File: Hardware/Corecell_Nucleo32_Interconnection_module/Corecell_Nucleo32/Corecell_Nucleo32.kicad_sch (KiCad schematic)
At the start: 3 parts, among them IC1 PCI_EXPRESS_CARD, J1 Conn_02x20_Odd_Even, U1 ESP32-DEVKITC-32D

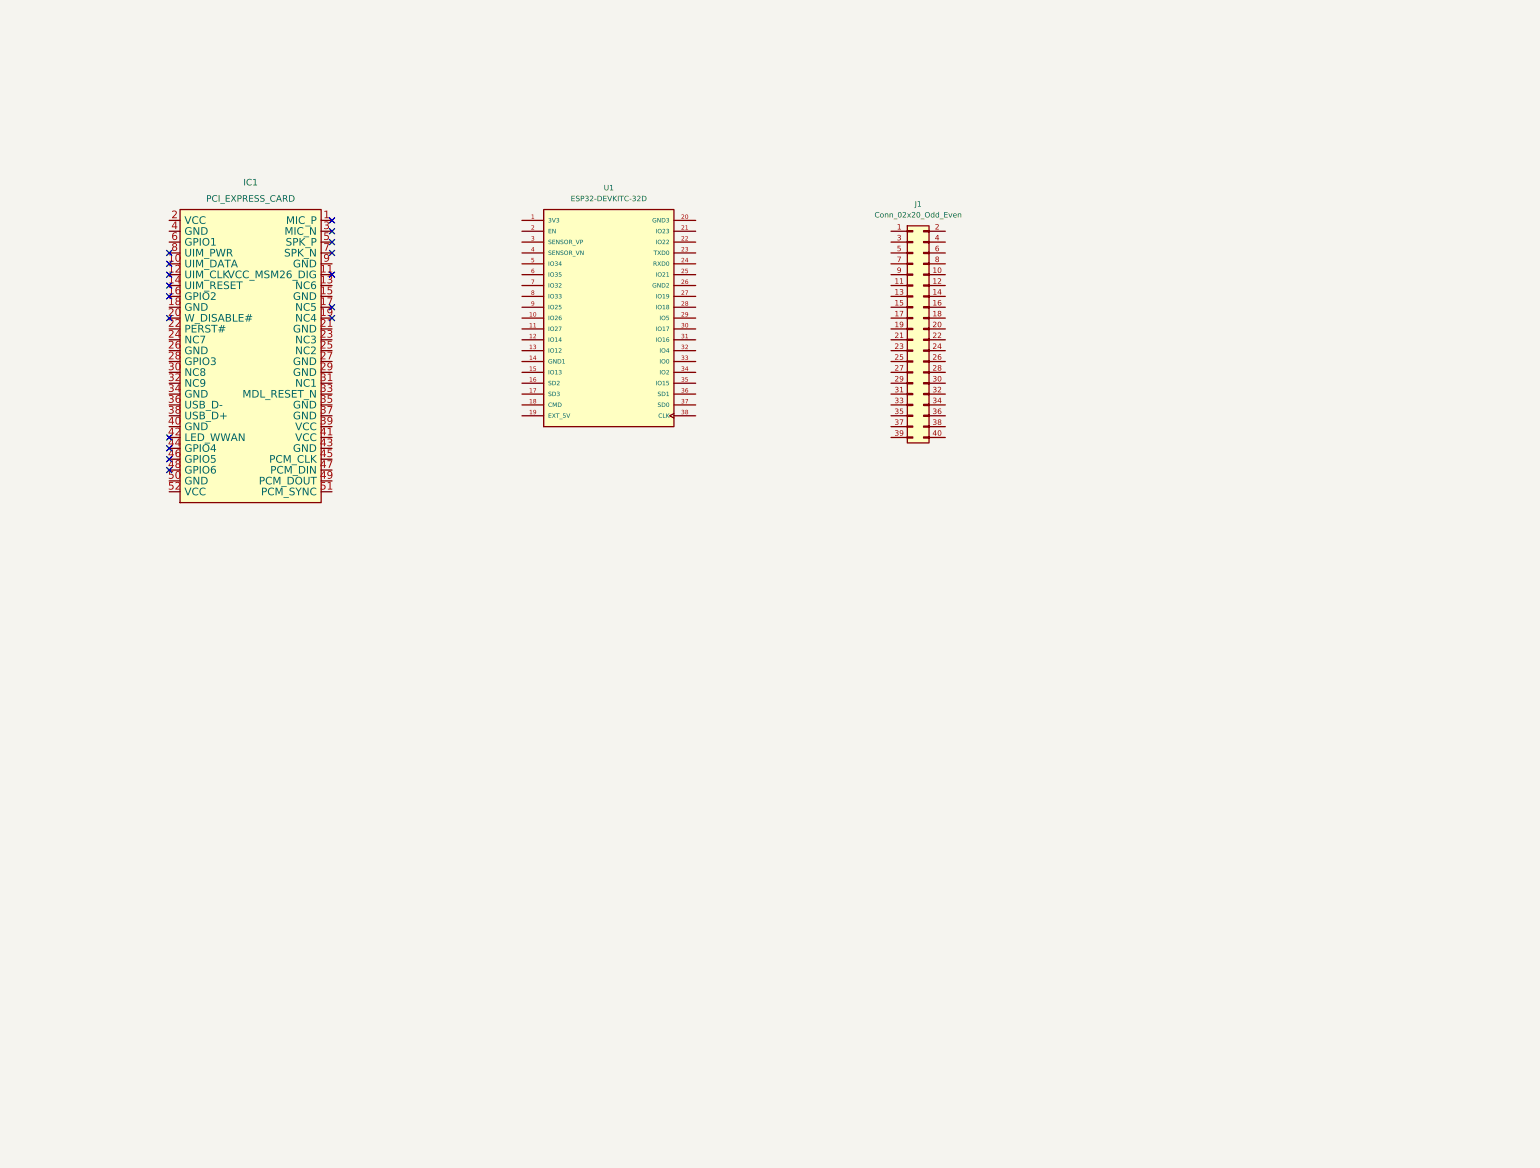
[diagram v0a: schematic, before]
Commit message: Some libs were made and added to schematic, the schematic is almost ready, fixing some warnings
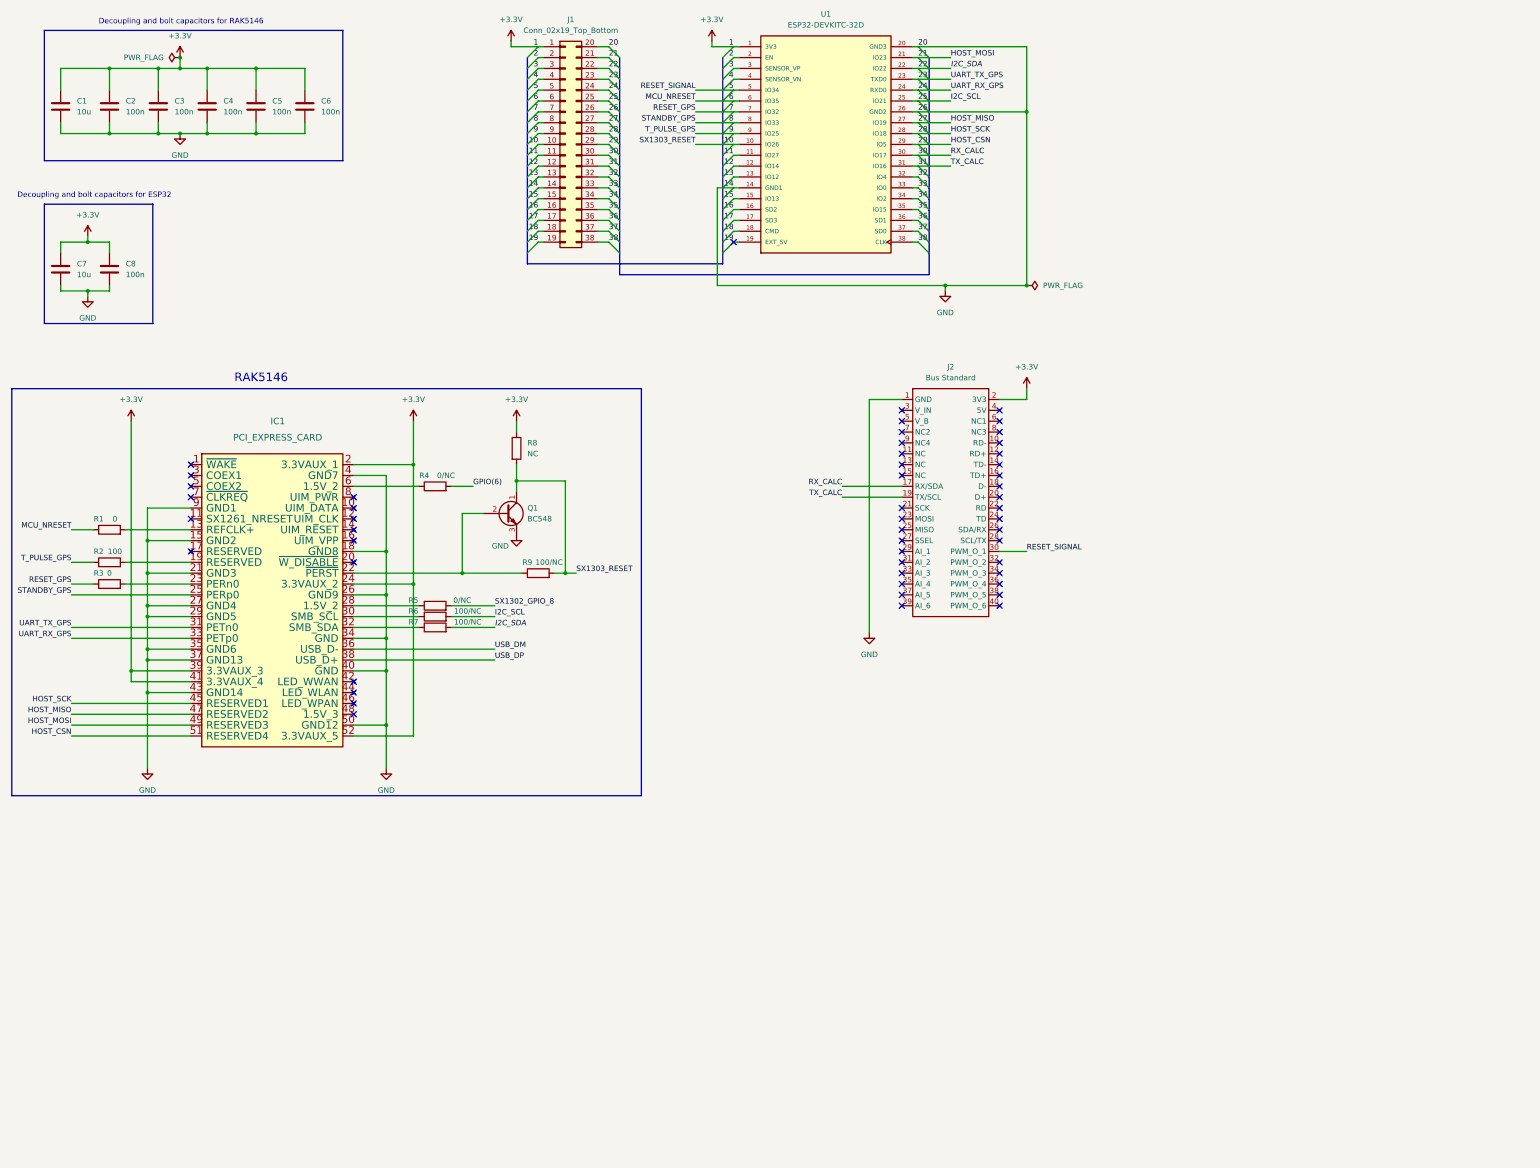
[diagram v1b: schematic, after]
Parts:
- removed J1: Conn_02x20_Odd_Even, symbol Connector_Generic:Conn_02x20_Odd_Even
- added C1, C7: 10u, symbol Device:C
- added C2, C3, C4, C5, C6, C8: 100n, symbol Device:C
- added J1: Conn_02x19_Top_Bottom, symbol Connector_Generic:Conn_02x19_Top_Bottom
- added J2: Bus Standard, symbol Corecell_Intercon_Board:Flatsat_conn
- added Q1: BC548, Package_TO_SOT_THT:TO-92_Inline, symbol Transistor_BJT:BC548
- added R1, R3: 0, symbol Device:R
- added R2: 100, symbol Device:R
- added R4, R5: 0/NC, symbol Device:R
- added R6, R7, R9: 100/NC, symbol Device:R
- added R8: NC, symbol Device:R
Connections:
- net +3V3: now reaches U1.1 (3V3)
- net +3V3: now also IC1.2 (3.3VAUX_1), IC1.24 (3.3VAUX_2), IC1.39 (3.3VAUX_3), IC1.41 (3.3VAUX_4), IC1.52 (3.3VAUX_5), C1.1, C2.1, C3.1, C4.1, C5.1, C6.1, C7.1, C8.1, J1.1 (Pin_1), J2.2 (3V3), R8.1
- net 10: now reaches U1.10 (IO26)
- net 10: now also J1.10 (Pin_10), Q1.1 (C), R8.2, R9.2
- net 11: now reaches U1.11 (IO27)
- net 11: now also J1.11 (Pin_11)
- net 12: now reaches U1.12 (IO14)
- net 12: now also J1.12 (Pin_12)
- net 13: now reaches U1.13 (IO12)
- net 13: now also J1.13 (Pin_13)
- net GND: now reaches U1.14 (GND1)
- net GND: now also IC1.15 (GND2), IC1.18 (GND8), IC1.21 (GND3), IC1.26 (GND9), IC1.27 (GND4), IC1.29 (GND5), IC1.34 (GND), IC1.35 (GND6), IC1.37 (GND13), IC1.4 (GND7), IC1.40 (GND), IC1.43 (GND14), IC1.50 (GND12), IC1.9 (GND1), U1.20 (GND3), U1.26 (GND2), C1.2, C2.2, C3.2, C4.2, C5.2, C6.2, C7.2, C8.2, J1.14 (Pin_14), J1.20 (Pin_20), J1.26 (Pin_26), J2.1 (GND), Q1.3 (E)
- net 15: now reaches U1.15 (IO13)
- net 15: now also J1.15 (Pin_15)
- net 16: now reaches U1.16 (SD2)
- net 16: now also J1.16 (Pin_16)
- net 17: now reaches U1.17 (SD3)
- net 17: now also J1.17 (Pin_17)
- net 18: now reaches U1.18 (CMD)
- net 18: now also J1.18 (Pin_18)
- net 19: now reaches U1.19 (EXT_5V)
- net 19: now also J1.19 (Pin_19)
- net 2: now reaches U1.2 (EN)
- net 2: now also J1.2 (Pin_2)
- net 21: now reaches U1.21 (IO23)
- net 21: now also IC1.49 (RESERVED3), J1.21 (Pin_21)
- net 22: now reaches U1.22 (IO22)
- net 22: now also J1.22 (Pin_22), R7.2
- net 23: now reaches U1.23 (TXD0)
- net 23: now also IC1.31 (PETn0), J1.23 (Pin_23)
- net 24: now reaches U1.24 (RXD0)
- net 24: now also IC1.33 (PETp0), J1.24 (Pin_24)
- net 25: now reaches U1.25 (IO21)
- net 25: now also J1.25 (Pin_25), R6.2
- net 27: now reaches U1.27 (IO19)
- net 27: now also IC1.47 (RESERVED2), J1.27 (Pin_27)
- net 28: now reaches U1.28 (IO18)
- net 28: now also IC1.45 (RESERVED1), J1.28 (Pin_28)
- net 29: now reaches U1.29 (IO5)
- net 29: now also IC1.51 (RESERVED4), J1.29 (Pin_29)
- net 3: now reaches U1.3 (SENSOR_VP)
- net 3: now also J1.3 (Pin_3)
- net 30: now reaches U1.30 (IO17)
- net 30: now also J1.30 (Pin_30), J2.17 (RX/SDA)
- net 31: now reaches U1.31 (IO16)
- net 31: now also J1.31 (Pin_31), J2.19 (TX/SCL)
- net 32: now reaches U1.32 (IO4)
- net 32: now also J1.32 (Pin_32)
- net 33: now reaches U1.33 (IO0)
- net 33: now also J1.33 (Pin_33)
- net 34: now reaches U1.34 (IO2)
- net 34: now also J1.34 (Pin_34)
- net 35: now reaches U1.35 (IO15)
- net 35: now also J1.35 (Pin_35)
- net 36: now reaches U1.36 (SD1)
- net 36: now also J1.36 (Pin_36)
- net 37: now reaches U1.37 (SD0)
- net 37: now also J1.37 (Pin_37)
- net 38: now reaches U1.38 (CLK)
- net 38: now also J1.38 (Pin_38)
- net 4: now reaches U1.4 (SENSOR_VN)
- net 4: now also J1.4 (Pin_4)
- net 5: now reaches U1.5 (IO34)
- net 5: now also J1.5 (Pin_5), J2.30 (PWM_O_1)
- net 6: now reaches U1.6 (IO35)
- net 6: now also J1.6 (Pin_6), R1.1
- net 7: now reaches U1.7 (IO32)
- net 7: now also J1.7 (Pin_7), R3.1
- net 8: now reaches U1.8 (IO33)
- net 8: now also IC1.25 (PERp0), J1.8 (Pin_8)
- net 9: now reaches U1.9 (IO25)
- net 9: now also J1.9 (Pin_9), R2.1
- net at IC1.13 (REFCLK+): now also R1.2
- net at IC1.19 (RESERVED): now also R2.2
- net at IC1.22 (~{PERST}): now also Q1.2 (B), R9.1
- net at IC1.23 (PERn0): now also R3.2
- net at IC1.28 (1.5V_2): now also R5.1
- net at IC1.30 (SMB_SCL): now also R6.1
- net at IC1.32 (SMB_SDA): now also R7.1
- net USB_DM: now reaches IC1.36 (USB_D-)
- net USB_DP: now reaches IC1.38 (USB_D+)
- net at IC1.6 (1.5V_2): now also R4.1
- new net GPIO(6): R4.2
- new net SX1302_GPIO_8: R5.2
- no-connect marks 17 -> 52
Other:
- note added: "Decoupling and bolt capacitors for ESP32"
- note added: "Decoupling and bolt capacitors for RAK5146"
- note added: "RAK5146"
- moved on the sheet: U1

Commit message: The base of schematic is completly connected, there is no error, no warning neither by ERC. After some debug connector will be added to give access to some critic connections points, like UART and others.
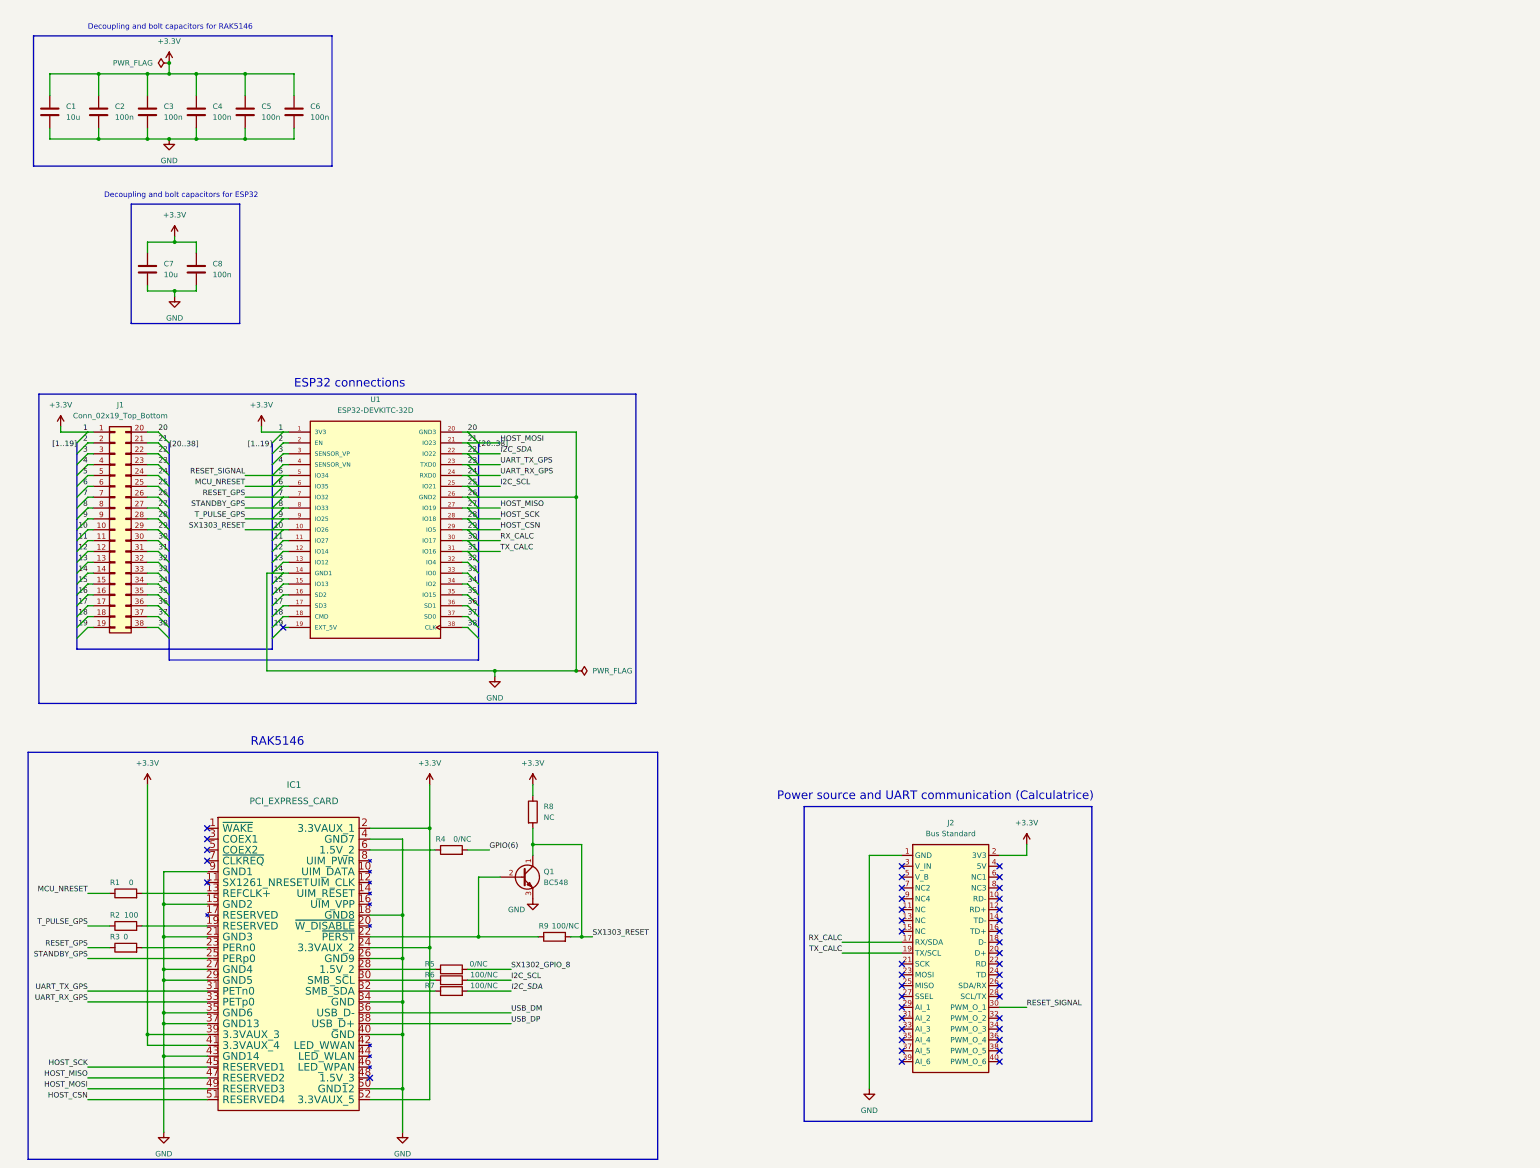
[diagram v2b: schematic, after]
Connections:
- no-connect marks 52 -> 42
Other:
- note added: "ESP32 connections"
- note added: "Power source and UART communication (Calculatrice)"
- moved on the sheet: C1, C2, C3, C4, C5, C6, C7, C8, IC1, J1, Q1, R1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

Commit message: Communication debug grooves were added. Some reset jumpers also
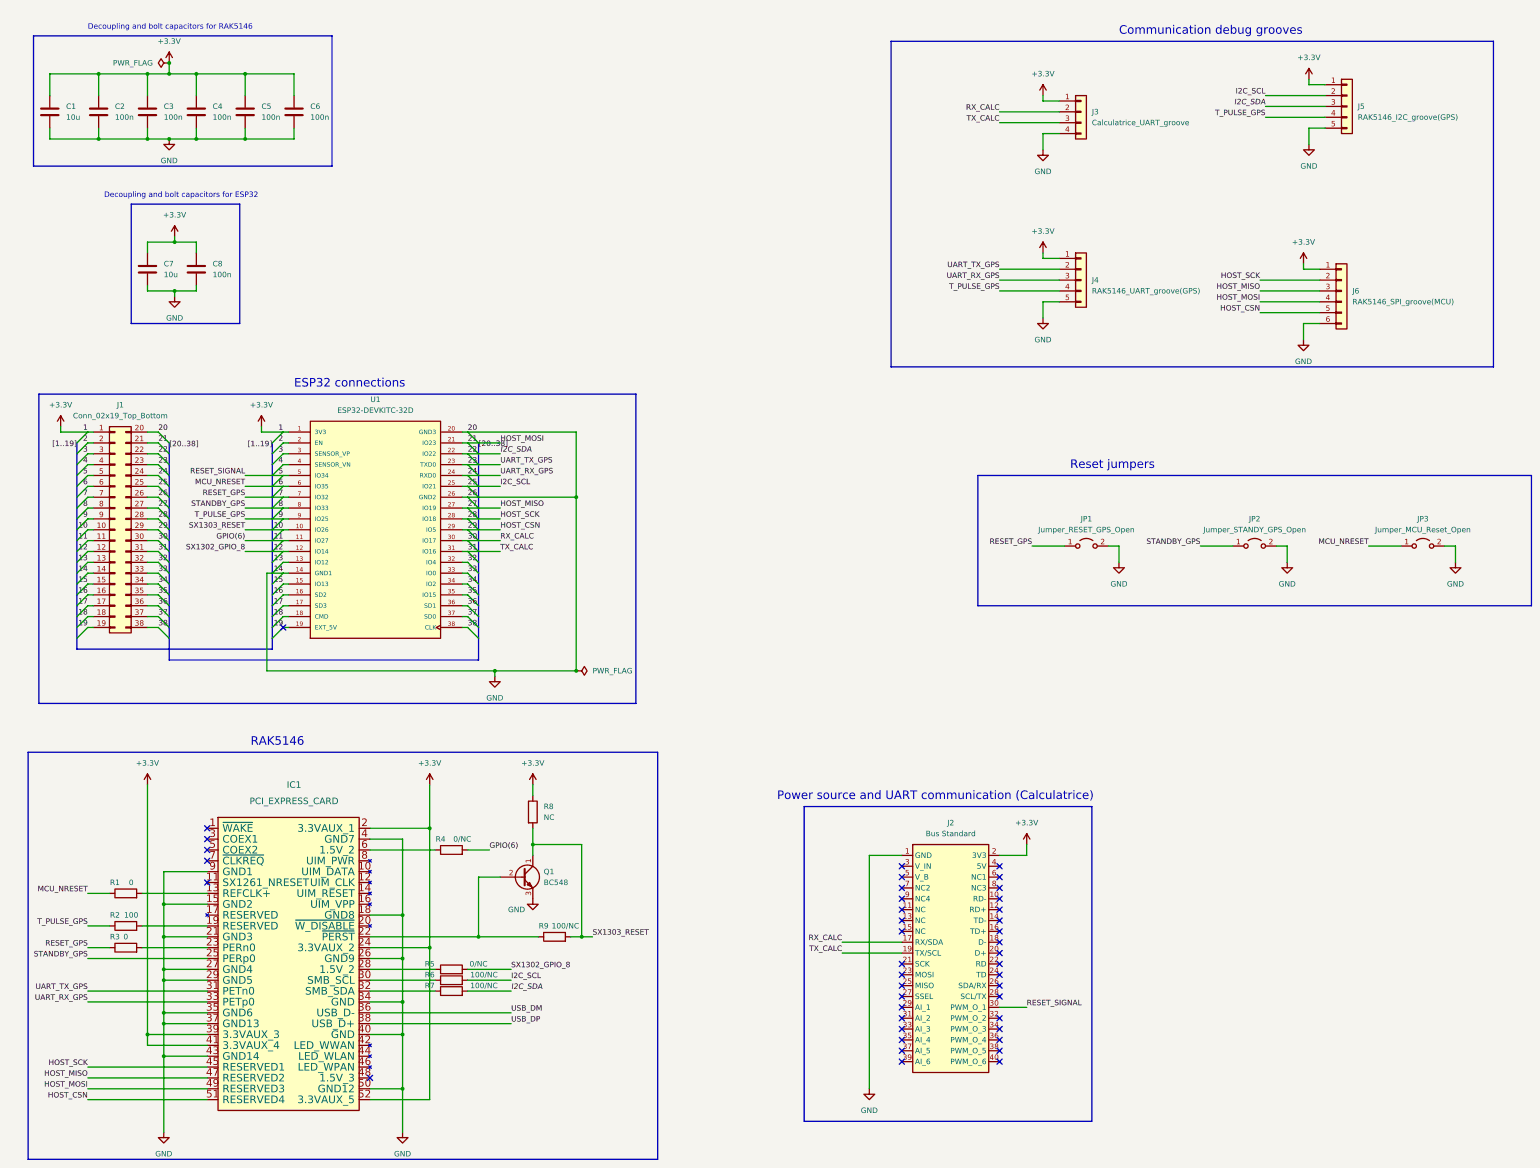
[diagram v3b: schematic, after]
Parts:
- added J3: Calculatrice_UART_groove, symbol Connector_Generic:Conn_01x04
- added J4: RAK5146_UART_groove(GPS), symbol Connector_Generic:Conn_01x05
- added J5: RAK5146_I2C_groove(GPS), symbol Connector_Generic:Conn_01x05
- added J6: RAK5146_SPI_groove(MCU), symbol Connector_Generic:Conn_01x06
- added JP1: Jumper_RESET_GPS_Open, symbol Jumper:Jumper_2_Open
- added JP2: Jumper_STANDY_GPS_Open, symbol Jumper:Jumper_2_Open
- added JP3: Jumper_MCU_Reset_Open, symbol Jumper:Jumper_2_Open
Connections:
- net GPIO(6) is gone; now on net 11: R4.2
- net SX1302_GPIO_8 is gone; now on net 12: R5.2
- net +3V3: now also J3.1 (Pin_1), J4.1 (Pin_1), J5.1 (Pin_1), J6.1 (Pin_1)
- net 21: now also J6.4 (Pin_4)
- net 22: now also J5.3 (Pin_3)
- net 23: now also J4.2 (Pin_2)
- net 24: now also J4.3 (Pin_3)
- net 25: now also J5.2 (Pin_2)
- net 27: now also J6.3 (Pin_3)
- net 28: now also J6.2 (Pin_2)
- net 29: now also J6.5 (Pin_5)
- net 30: now also J3.2 (Pin_2)
- net 31: now also J3.3 (Pin_3)
- net 6: now also JP3.1 (A)
- net 7: now also JP1.1 (A)
- net 8: now also JP2.1 (A)
- net 9: now also J4.4 (Pin_4), J5.4 (Pin_4)
- net GND: now also J3.4 (Pin_4), J4.5 (Pin_5), J5.5 (Pin_5), J6.6 (Pin_6), JP1.2 (B), JP2.2 (B), JP3.2 (B)
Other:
- note added: "Communication debug grooves"
- note added: "Reset jumpers"
